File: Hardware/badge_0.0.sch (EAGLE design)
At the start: 42 parts, among them CON1 PH_2, IC1 CP2102, SW1 MK12C02, SW2 MK12C02, U4 MCP73832T-2DCI/OT

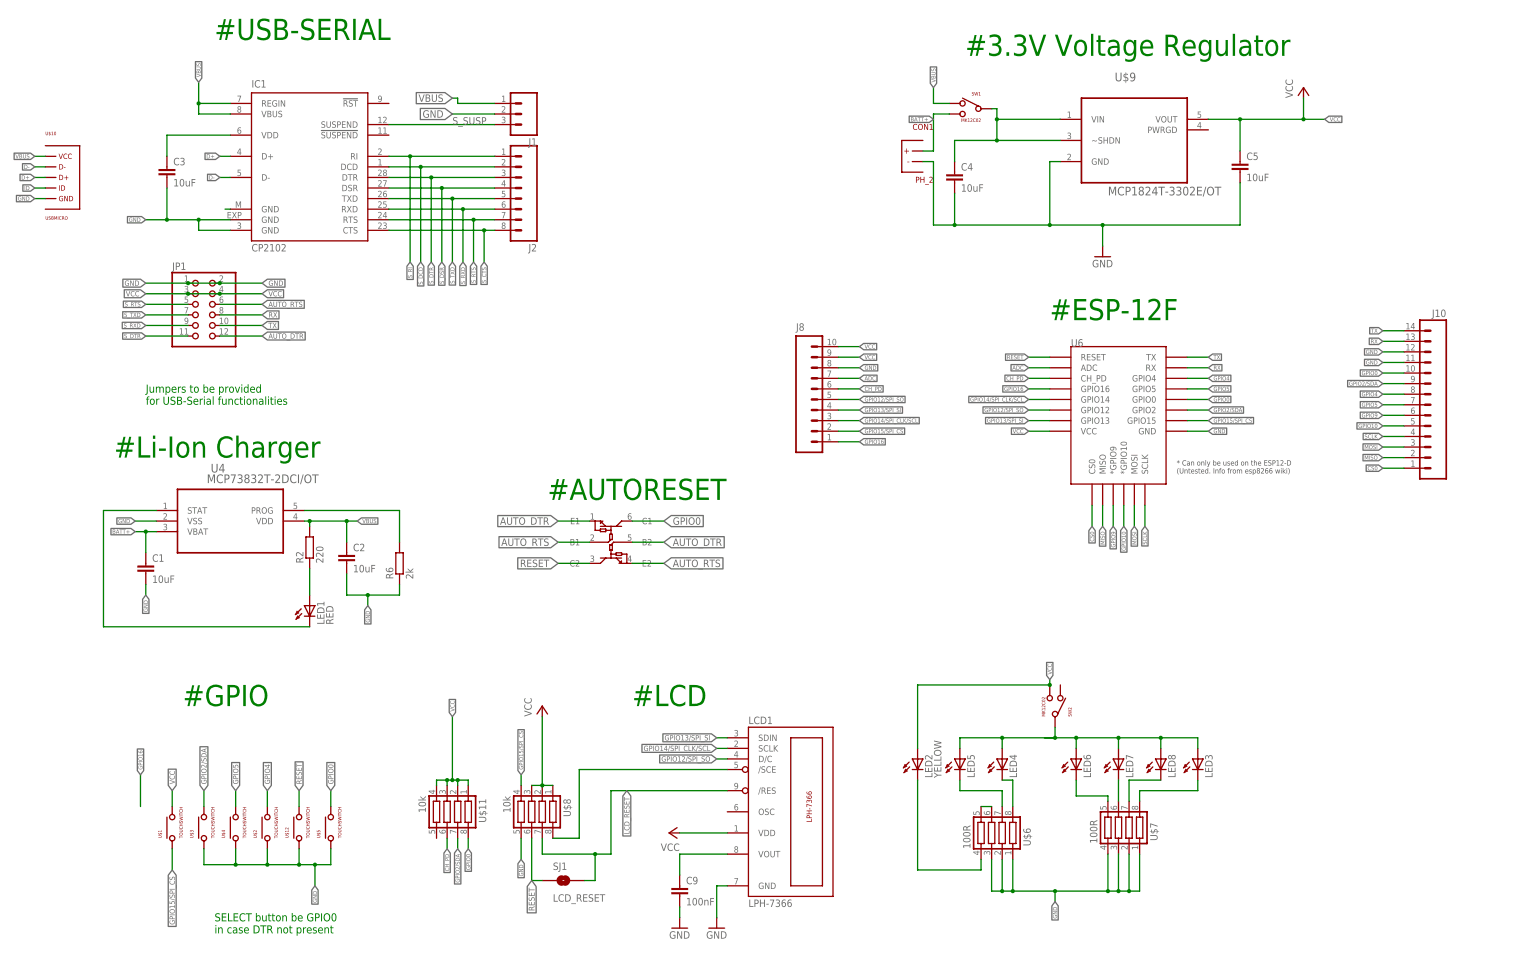
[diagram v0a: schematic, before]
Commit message: Added snapoffable USB-serial
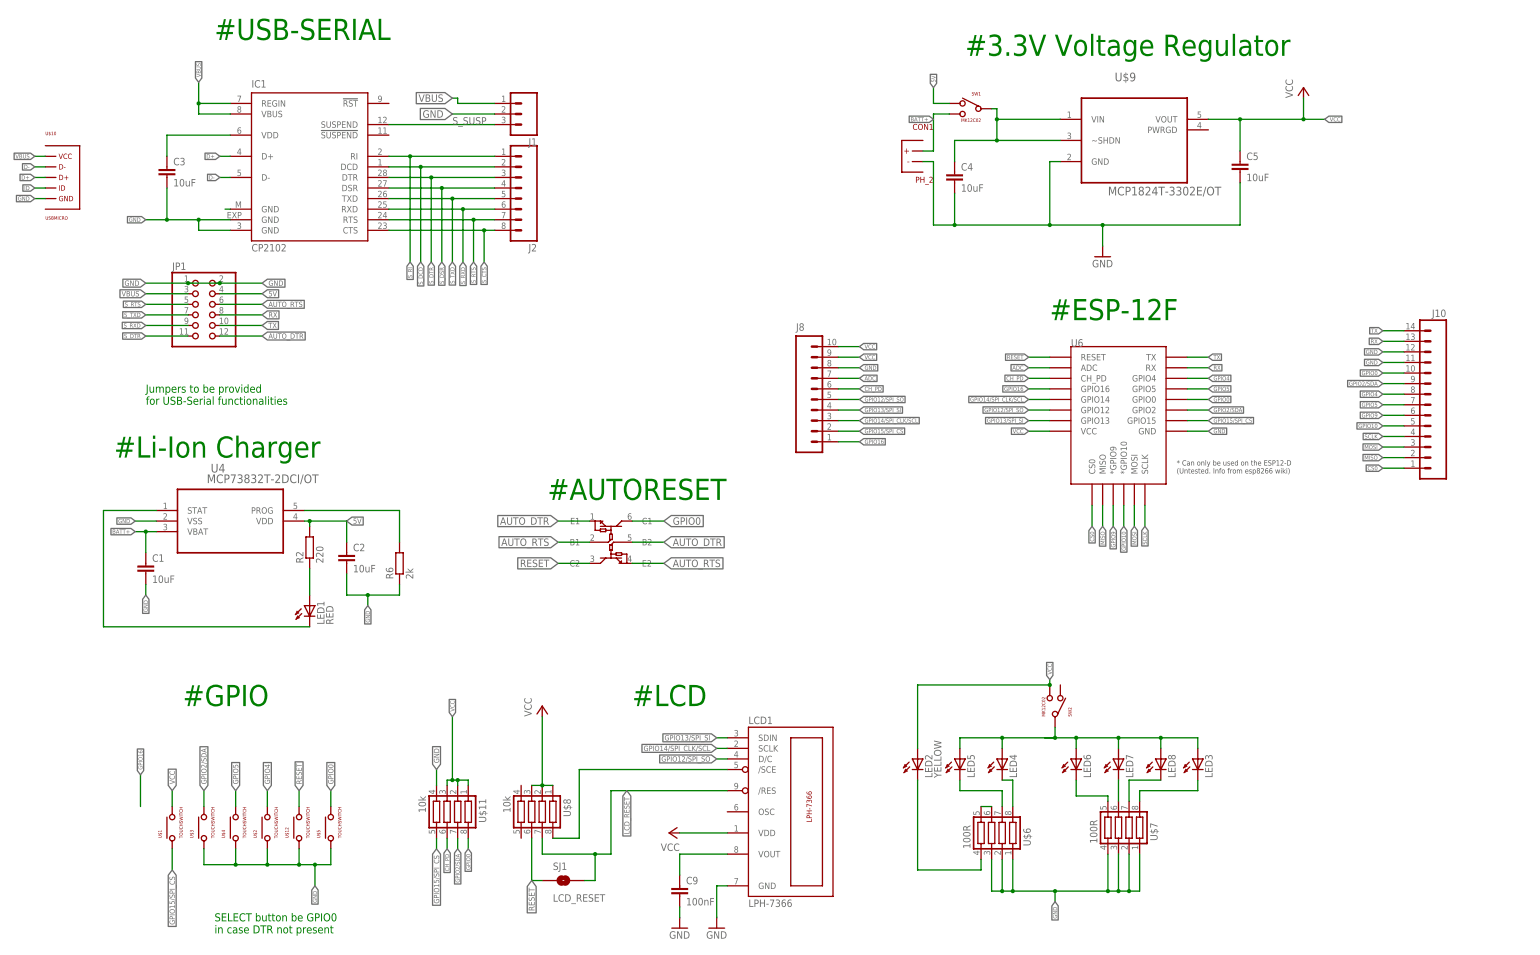
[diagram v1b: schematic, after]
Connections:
- new net 5V: C2.1, JP1.4, R2.2, SW1.P$2, U4.VDD
- net GND: now also U$11.4; no longer U$8.5
- net GPIO15/SPI_CS: now also U$11.5; no longer U$8.4
- net VBUS: now also JP1.3; no longer C2.1, R2.2, SW1.P$2, U4.VDD
- net VCC: no longer JP1.3, JP1.4, U$11.4
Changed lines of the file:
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@@
 <?xml version="1.0" encoding="utf-8"?>
 <!DOCTYPE eagle SYSTEM "eagle.dtd">
-<eagle version="7.5.0">
+<eagle version="7.1.0">
 <drawing>
 <settings>
@@
 <setting verticaltext="up"/>
 </settings>
-<grid distance="0.1" unitdist="inch" unit="inch" style="lines" multiple="1" display="no" altdistance="0.01" altunitdist="inch" altunit="inch"/>
+<grid distance="0.05" unitdist="inch" unit="inch" style="lines" multiple="1" display="yes" altdistance="0.025" altunitdist="inch" altunit="inch"/>
 <layers>
 <layer number="1" name="Top" color="4" fill="1" visible="no" active="no"/>
@@
 <segment>
 <label x="116.84" y="81.28" size="1.016" layer="95" rot="R90" xref="yes"/>
-<pinref part="U$11" gate="G$1" pin="4"/>
-<wire x1="113.03" y1="64.77" x2="113.03" y2="66.04" width="0.1524" layer="91"/>
-<wire x1="113.03" y1="66.04" x2="115.57" y2="66.04" width="0.1524" layer="91"/>
 <pinref part="U$11" gate="G$1" pin="1"/>
 <wire x1="115.57" y1="66.04" x2="116.84" y2="66.04" width="0.1524" layer="91"/>
@@
 <pinref part="U$11" gate="G$1" pin="3"/>
 <wire x1="115.57" y1="66.04" x2="115.57" y2="64.77" width="0.1524" layer="91"/>
-<junction x="115.57" y="66.04"/>
 <junction x="116.84" y="66.04"/>
 <wire x1="116.84" y1="66.04" x2="116.84" y2="81.28" width="0.1524" layer="91"/>
@@
 <wire x1="49.53" y1="59.69" x2="49.53" y2="63.5" width="0.1524" layer="91"/>
 <label x="49.53" y="63.5" size="1.27" layer="95" rot="R90" xref="yes"/>
-</segment>
-<segment>
-<wire x1="60.96" y1="182.88" x2="71.12" y2="182.88" width="0.1524" layer="91"/>
-<label x="71.12" y="182.88" size="1.27" layer="95" xref="yes"/>
-<pinref part="JP1" gate="A" pin="4"/>
-<pinref part="JP1" gate="A" pin="3"/>
-<wire x1="53.34" y1="182.88" x2="60.96" y2="182.88" width="0.1524" layer="91"/>
-<junction x="60.96" y="182.88"/>
-<wire x1="53.34" y1="182.88" x2="43.18" y2="182.88" width="0.1524" layer="91"/>
-<junction x="53.34" y="182.88"/>
-<label x="43.18" y="182.88" size="1.27" layer="95" rot="R180" xref="yes"/>
 </segment>
 </net>
@@
 <wire x1="345.44" y1="168.91" x2="340.36" y2="168.91" width="0.1524" layer="91"/>
 <label x="340.36" y="168.91" size="1.016" layer="95" rot="R180" xref="yes"/>
-</segment>
-<segment>
-<wire x1="133.35" y1="46.99" x2="133.35" y2="52.07" width="0.1524" layer="91"/>
-<label x="133.35" y="46.99" size="1.016" layer="95" rot="R270" xref="yes"/>
-<pinref part="U$8" gate="G$1" pin="5"/>
 </segment>
 <segment>
@@
 <label x="43.18" y="185.42" size="1.27" layer="95" rot="R180" xref="yes"/>
 </segment>
+<segment>
+<pinref part="U$11" gate="G$1" pin="4"/>
+<wire x1="113.03" y1="64.77" x2="113.03" y2="68.58" width="0.1524" layer="91"/>
+<label x="113.03" y="68.58" size="1.27" layer="95" rot="R90" xref="yes"/>
+</segment>
 </net>
 <net name="N$3" class="0">
@@
 </segment>
 <segment>
-<label x="133.35" y="67.31" size="1.016" layer="95" rot="R90" xref="yes"/>
-<pinref part="U$8" gate="G$1" pin="4"/>
-<wire x1="133.35" y1="64.77" x2="133.35" y2="67.31" width="0.1524" layer="91"/>
+<pinref part="U$11" gate="G$1" pin="5"/>
+<wire x1="113.03" y1="52.07" x2="113.03" y2="49.53" width="0.1524" layer="91"/>
+<label x="113.03" y="49.53" size="1.27" layer="95" rot="R270" xref="yes"/>
 </segment>
 </net>
 <net name="VBUS" class="0">
-<segment>
-<wire x1="232.41" y1="228.6" x2="232.41" y2="232.41" width="0.1524" layer="91"/>
-<label x="232.41" y="232.41" size="1.016" layer="95" rot="R90" xref="yes"/>
-<pinref part="SW1" gate="G$1" pin="P$2"/>
-<wire x1="236.22" y1="228.6" x2="232.41" y2="228.6" width="0.1524" layer="91"/>
-</segment>
 <segment>
 <pinref part="U$10" gate="G$1" pin="P$VCC"/>
 <wire x1="16.51" y1="215.9" x2="19.05" y2="215.9" width="0.1524" layer="91"/>
 <label x="16.51" y="215.9" size="1.016" layer="95" rot="R180" xref="yes"/>
-</segment>
-<segment>
-<pinref part="U4" gate="A" pin="VDD"/>
-<label x="93.98" y="128.27" size="1.016" layer="95" xref="yes"/>
-<wire x1="81.28" y1="128.27" x2="82.55" y2="128.27" width="0.1524" layer="91"/>
-<wire x1="82.55" y1="127" x2="82.55" y2="128.27" width="0.1524" layer="91"/>
-<wire x1="82.55" y1="128.27" x2="91.44" y2="128.27" width="0.1524" layer="91"/>
-<wire x1="91.44" y1="128.27" x2="93.98" y2="128.27" width="0.1524" layer="91"/>
-<pinref part="C2" gate="G$1" pin="1"/>
-<wire x1="91.44" y1="128.27" x2="91.44" y2="123.19" width="0.1524" layer="91"/>
-<junction x="91.44" y="128.27"/>
-<pinref part="R2" gate="G$1" pin="2"/>
-<junction x="82.55" y="128.27"/>
 </segment>
 <segment>
@@
 <wire x1="118.11" y1="229.87" x2="116.84" y2="229.87" width="0.1524" layer="91"/>
 <label x="116.84" y="229.87" size="1.778" layer="95" rot="R180" xref="yes"/>
+</segment>
+<segment>
+<pinref part="JP1" gate="A" pin="3"/>
+<wire x1="53.34" y1="182.88" x2="43.18" y2="182.88" width="0.1524" layer="91"/>
+<label x="43.18" y="182.88" size="1.27" layer="95" rot="R180" xref="yes"/>
 </segment>
 </net>
@@
 </segment>
 </net>
+<net name="5V" class="0">
+<segment>
+<wire x1="232.41" y1="228.6" x2="232.41" y2="232.41" width="0.1524" layer="91"/>
+<label x="232.41" y="232.41" size="1.016" layer="95" rot="R90" xref="yes"/>
+<pinref part="SW1" gate="G$1" pin="P$2"/>
+<wire x1="236.22" y1="228.6" x2="232.41" y2="228.6" width="0.1524" layer="91"/>
+</segment>
+<segment>
+<pinref part="JP1" gate="A" pin="4"/>
+<wire x1="60.96" y1="182.88" x2="71.12" y2="182.88" width="0.1524" layer="91"/>
+<label x="71.12" y="182.88" size="1.27" layer="95" xref="yes"/>
+</segment>
+<segment>
+<pinref part="U4" gate="A" pin="VDD"/>
+<pinref part="C2" gate="G$1" pin="1"/>
+<wire x1="81.28" y1="128.27" x2="82.55" y2="128.27" width="0.1524" layer="91"/>
+<wire x1="82.55" y1="128.27" x2="91.44" y2="128.27" width="0.1524" layer="91"/>
+<wire x1="91.44" y1="128.27" x2="91.44" y2="123.19" width="0.1524" layer="91"/>
+<pinref part="R2" gate="G$1" pin="2"/>
+<wire x1="82.55" y1="127" x2="82.55" y2="128.27" width="0.1524" layer="91"/>
+<junction x="82.55" y="128.27"/>
+<label x="91.44" y="128.27" size="1.27" layer="95" xref="yes"/>
+</segment>
+</net>

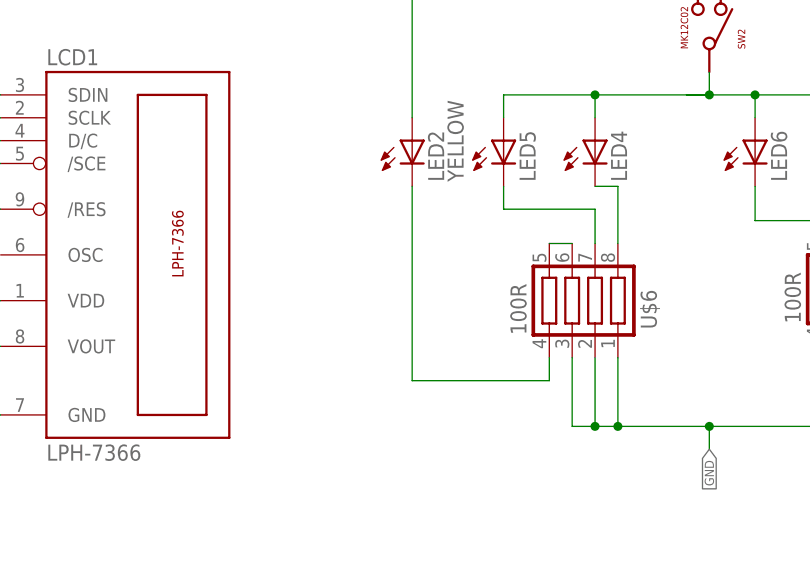
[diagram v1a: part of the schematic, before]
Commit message: Added SJ2 for power LED for reducing power usage
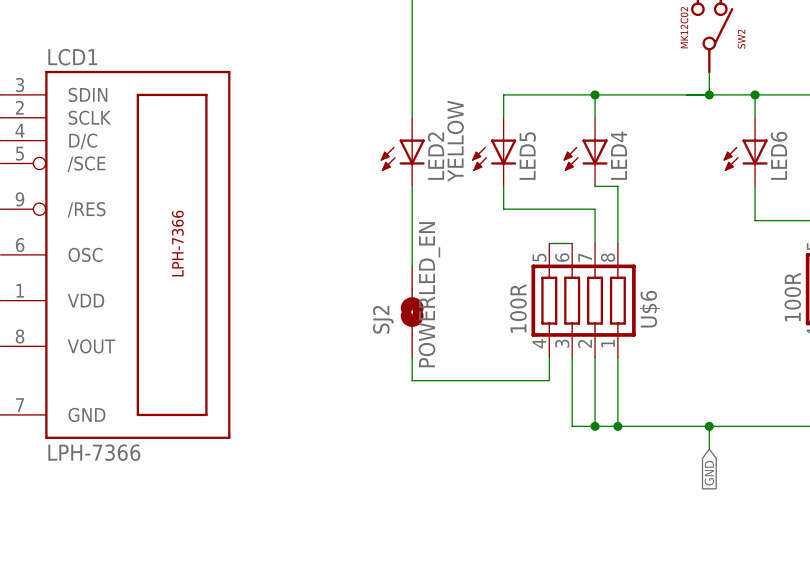
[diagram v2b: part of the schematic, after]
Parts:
- added SJ2: POWERLED_EN, SparkFun-Retired:SOLDERJUMPERTRACE
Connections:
- new net N$16: LED2.C, SJ2.2
- net N$15: now also SJ2.1; no longer LED2.C
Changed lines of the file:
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@@
 <setting verticaltext="up"/>
 </settings>
-<grid distance="0.05" unitdist="inch" unit="inch" style="lines" multiple="1" display="yes" altdistance="0.025" altunitdist="inch" altunit="inch"/>
+<grid distance="0.05" unitdist="inch" unit="inch" style="lines" multiple="1" display="yes" altdistance="0.01" altunitdist="inch" altunit="inch"/>
 <layers>
 <layer number="1" name="Top" color="4" fill="1" visible="no" active="no"/>
@@
 <part name="SJ1" library="SparkFun-Retired" deviceset="SOLDERJUMPER" device="TRACE" value="LCD_RESET"/>
 <part name="JP1" library="pinhead" deviceset="PINHD-2X6" device=""/>
+<part name="SJ2" library="SparkFun-Retired" deviceset="SOLDERJUMPER" device="TRACE" value="POWERLED_EN"/>
 </parts>
 <sheets>
@@
 <instance part="SJ1" gate="1" x="143.51" y="41.91"/>
 <instance part="JP1" gate="A" x="55.88" y="180.34"/>
+<instance part="SJ2" gate="1" x="228.6" y="52.07" smashed="yes" rot="R90">
+<attribute name="NAME" x="226.06" y="49.53" size="1.778" layer="95" rot="R90"/>
+<attribute name="VALUE" x="231.14" y="45.72" size="1.778" layer="96" rot="R90"/>
+</instance>
 </instances>
 <busses>
@@
 <segment>
 <pinref part="U$6" gate="G$1" pin="4"/>
-<pinref part="LED2" gate="G$1" pin="C"/>
-<wire x1="228.6" y1="66.04" x2="228.6" y2="44.45" width="0.1524" layer="91"/>
+<wire x1="228.6" y1="46.99" x2="228.6" y2="44.45" width="0.1524" layer="91"/>
 <wire x1="228.6" y1="44.45" x2="243.84" y2="44.45" width="0.1524" layer="91"/>
 <wire x1="243.84" y1="46.99" x2="243.84" y2="44.45" width="0.1524" layer="91"/>
+<pinref part="SJ2" gate="1" pin="1"/>
 </segment>
 </net>
@@
 </segment>
 </net>
+<net name="N$16" class="0">
+<segment>
+<pinref part="LED2" gate="G$1" pin="C"/>
+<wire x1="228.6" y1="66.04" x2="228.6" y2="57.15" width="0.1524" layer="91"/>
+<pinref part="SJ2" gate="1" pin="2"/>
+</segment>
+</net>
